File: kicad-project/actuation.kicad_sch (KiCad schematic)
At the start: 0 parts

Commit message: hw: schematic updates
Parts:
- added C? (x4): (no value), symbol Device:C
- added C?: (no value), symbol Device:C_Polarized
- added R? (x4): (no value), symbol Device:R
- added U?: (no value), symbol A4988:A4988SETTR-T
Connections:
- new net: R?.1, U?.13 (ROSC)
- new net: R?.1, U?.23 (SENSE1)
- new net: R?.1, U?.27 (SENSE2)
- new net: C?.1, U?.4 (CP1)
- new net: C?.2, U?.5 (CP2)
- new net: C?.1, U?.8 (VREG)
- new net +12V: C?.1, C?.1, U?.22 (VBB1), U?.28 (VBB2)
- new net +5V: C?.1, R?.1, U?.15 (VDD)
- new net GND: C?.2, C?.2, C?.2, R?.2, R?.2, R?.2, U?.18 (GND2), U?.3 (GND1)
- new net SLEEP: R?.2, U?.14 (~{SLEEP})
- new net VCP: C?.2, U?.6 (VCP)
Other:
- note added: "Al momento stiamo pilotando un motore unipolare Bisogna capire se questo driver supporta tali motori"
- note added: "DRV8805"
- note added: "e se bastano i pin"
- title: Actuation -> (none)

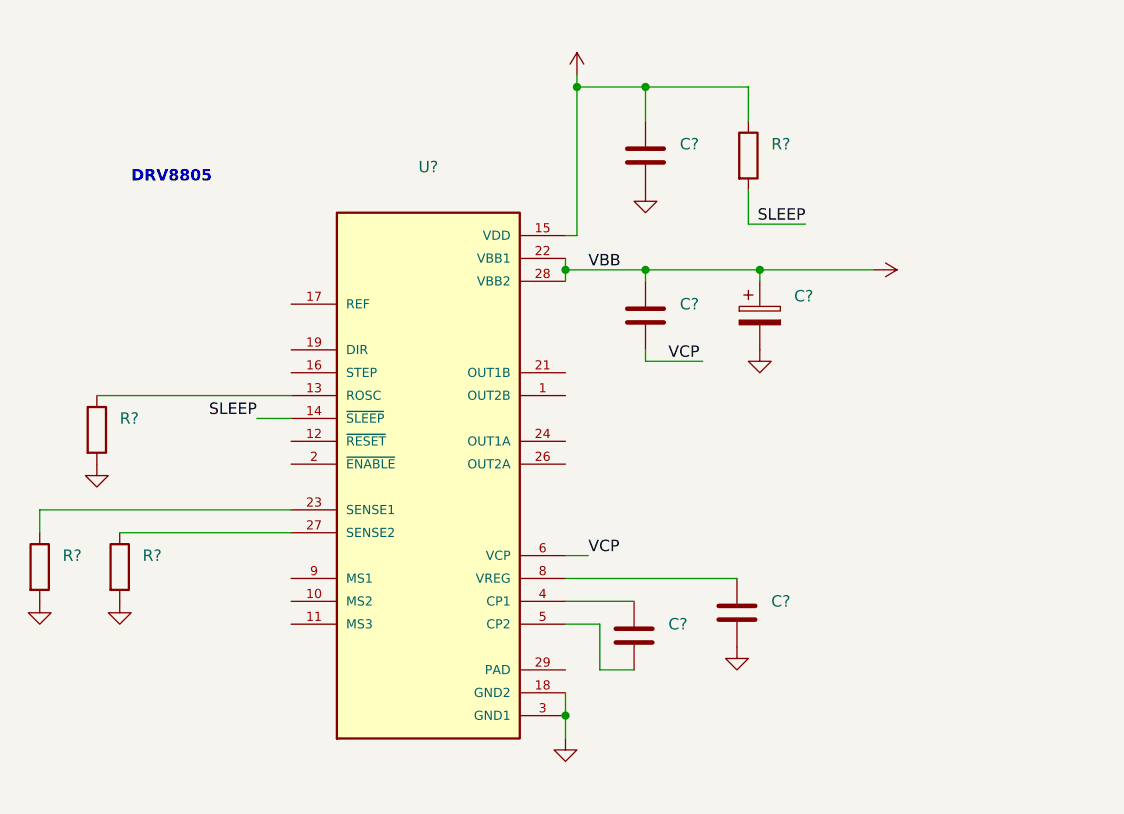
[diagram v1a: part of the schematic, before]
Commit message: hw: connect filtering capacitor near vdd pin
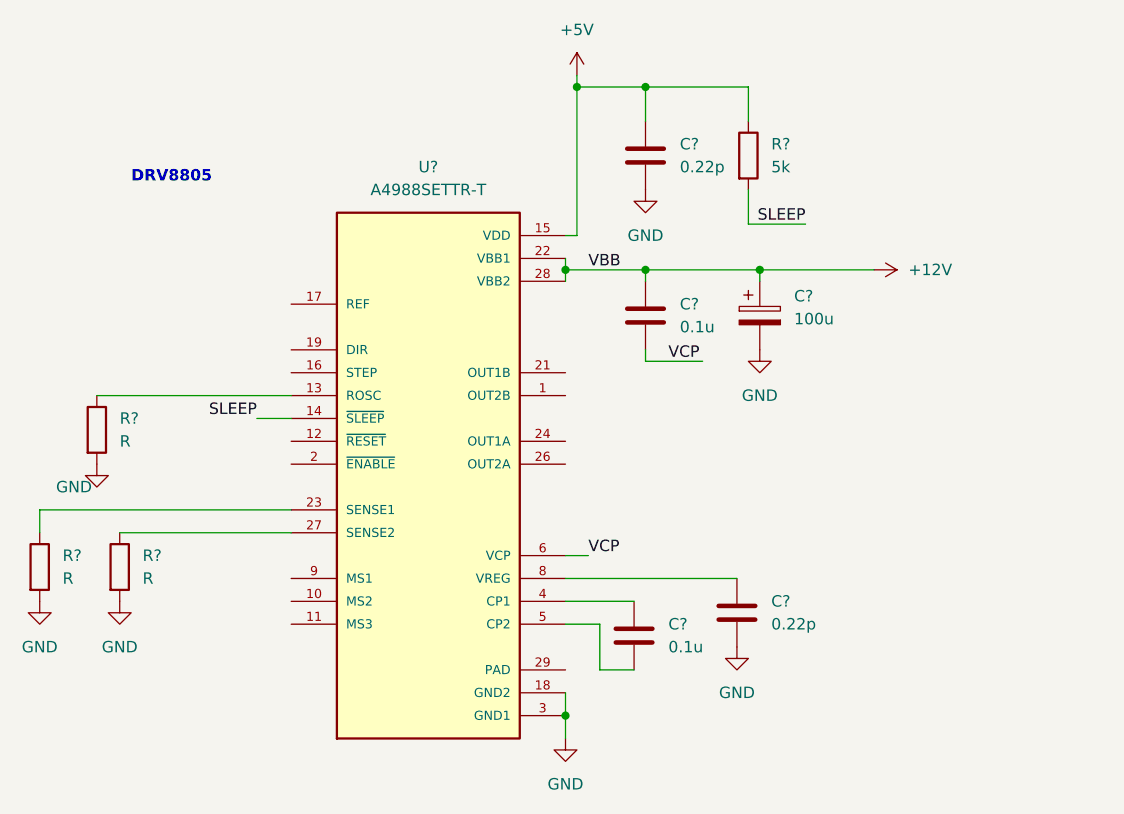
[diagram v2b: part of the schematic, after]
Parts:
- C? (x2): value (none) -> 0.22p
- C? (x2): value (none) -> 0.1u
- C?: value (none) -> 100u
- R? (x3): value (none) -> R
- R?: value (none) -> 5k
- U?: value (none) -> A4988SETTR-T; footprint (none) -> QFN50P500X500X90-29N

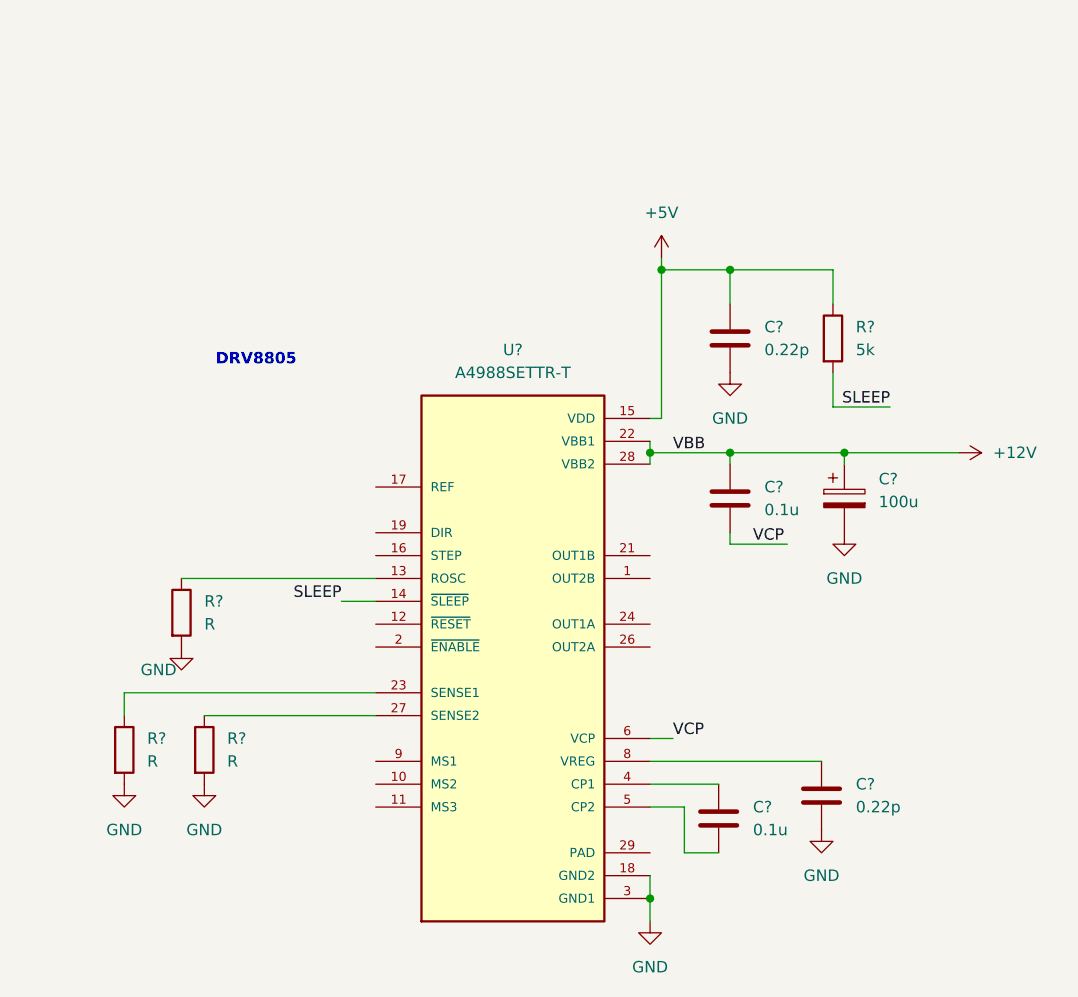
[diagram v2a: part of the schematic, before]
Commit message: hw: update schematic pt. 2
add switching enable resistor, change usb inductor to ferrite bead, add OR gate and microstepping solder jumpers to motor driver, remove i2c and backup supply solder jumper from GPS, add ferrite bead to GPS, remove limit switches and other small changes
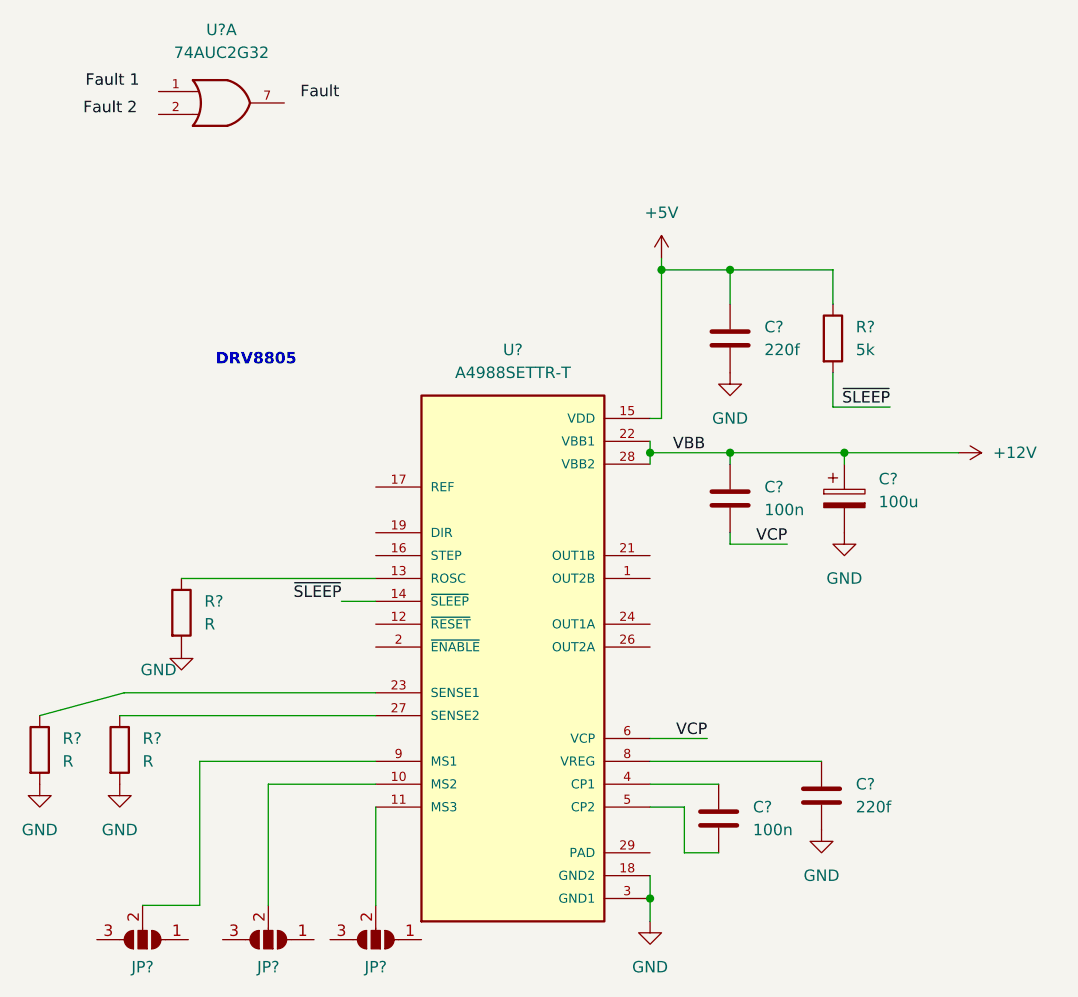
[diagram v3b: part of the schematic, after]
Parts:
- added JP? (x3): SolderJumper_3_Open, symbol Jumper:SolderJumper_3_Open
- added U?: 74AUC2G32, symbol 74xGxx:74AUC2G32
- C? (x2): value 0.22p -> 220f
- C? (x2): value 0.1u -> 100n
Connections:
- net GND: now also U?.4 (GND)
- net at U?.10 (MS2): now also JP?.2 (C)
- net at U?.11 (MS3): now also JP?.2 (C)
- net at U?.9 (MS1): now also JP?.2 (C)
- net SLEEP renamed ~{SLEEP}
- new net VCC: U?.8 (VCC)
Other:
- moved on the sheet: R?

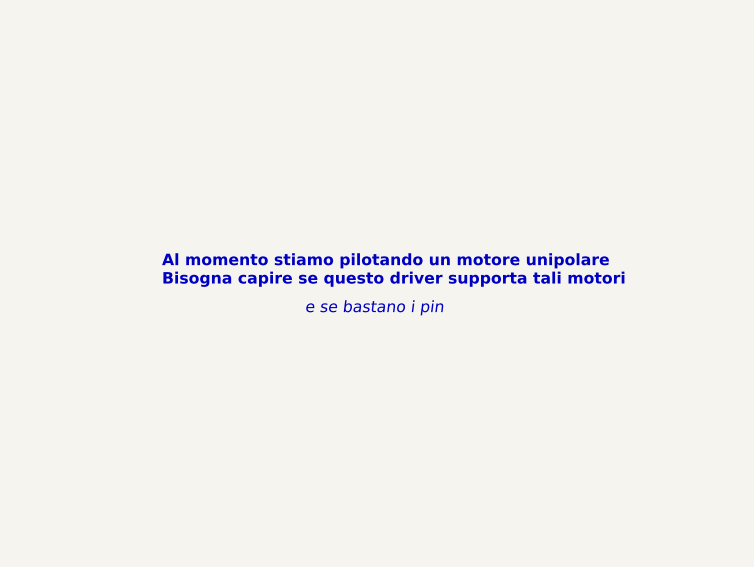
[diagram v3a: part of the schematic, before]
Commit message: hw: added MAN_NORD and TRCK_ON_OFF buttons and OLED Display
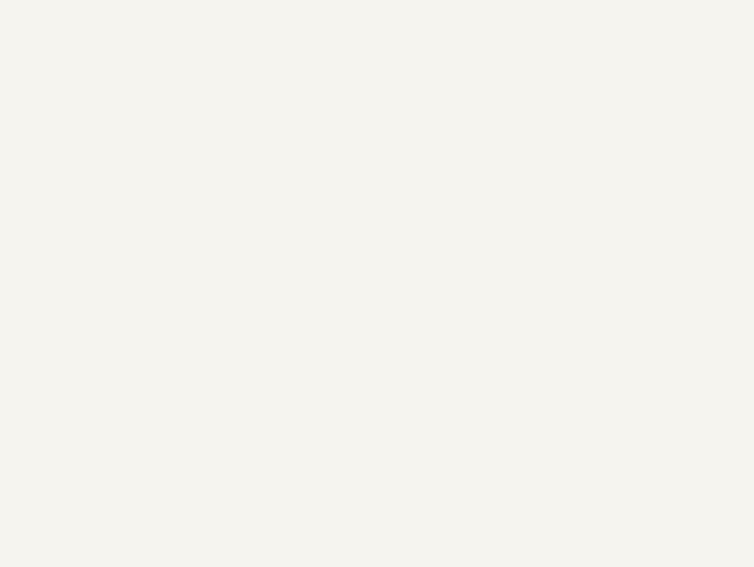
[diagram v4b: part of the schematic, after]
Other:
- note removed: "Al momento stiamo pilotando un motore unipolare Bisogna capire se questo driver supporta tali motori"
- note removed: "e se bastano i pin"

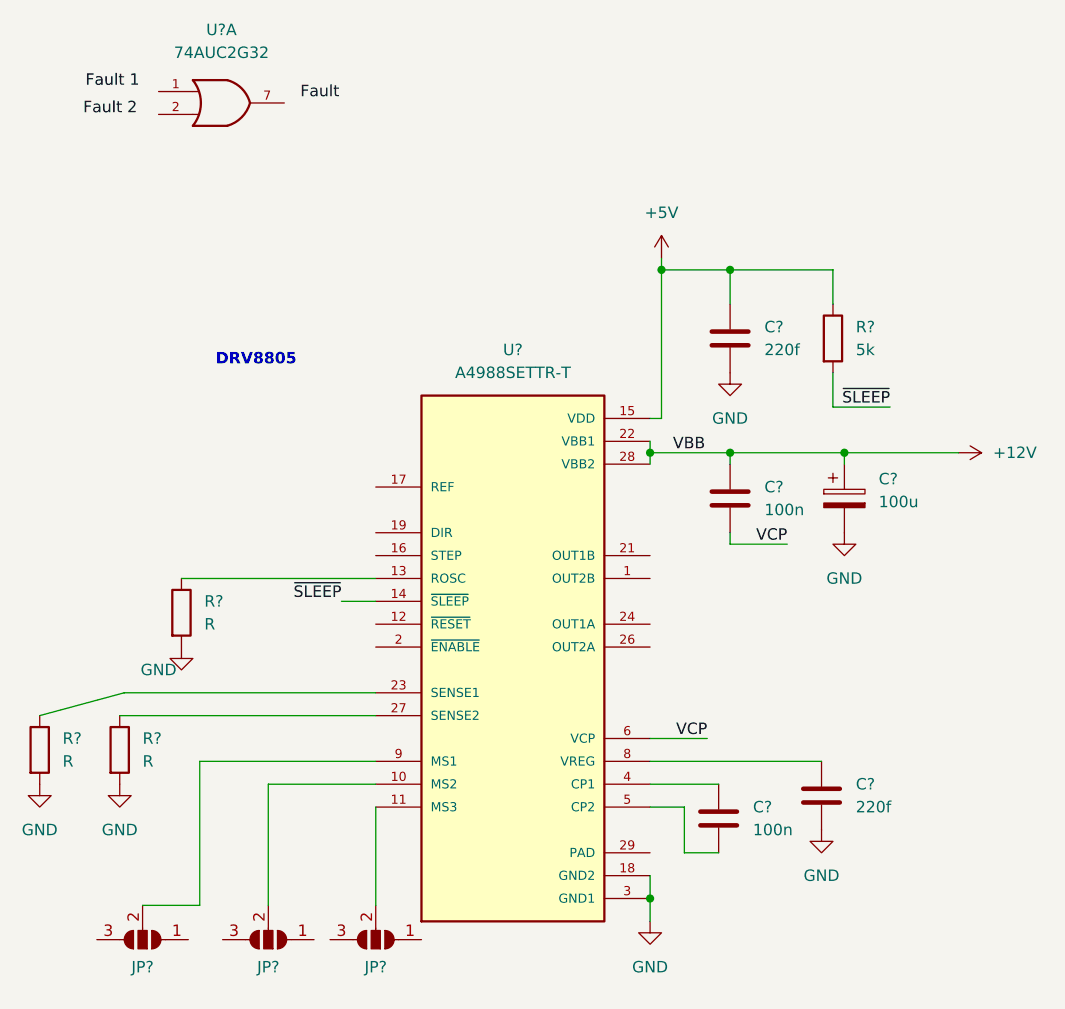
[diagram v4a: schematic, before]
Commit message: hw: set grid to 50 mils and missing labels
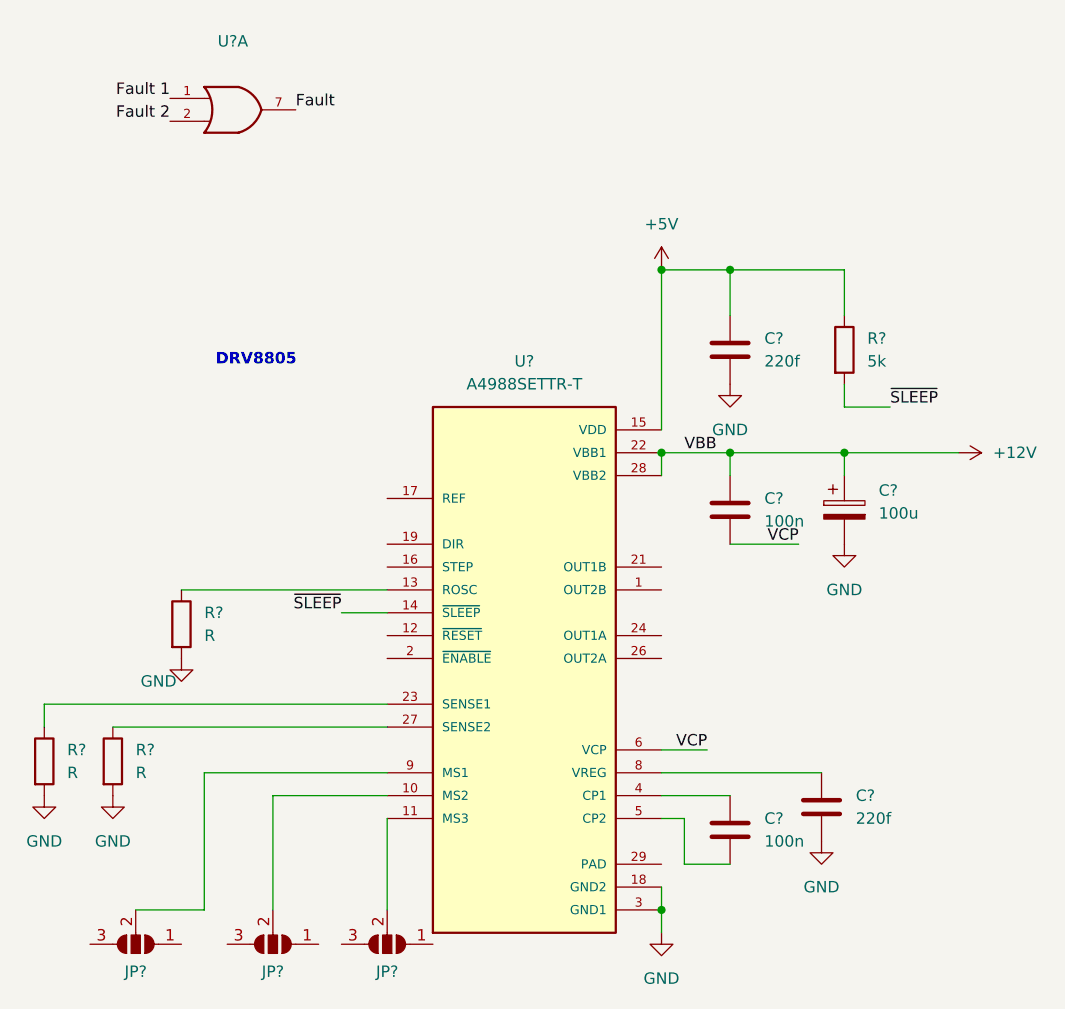
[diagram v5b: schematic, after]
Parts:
- removed U?: 74AUC2G32, symbol 74xGxx:74AUC2G32
- added U?: (no value), symbol 74xGxx:74AUC2G32
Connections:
- net Fault: now also U?.7
- net Fault 1: now also U?.1
- net Fault 2: now also U?.2
- net GND: now also U?.4 (GND)
- net VCC: now also U?.8 (VCC)
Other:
- moved on the sheet: C?, JP?, R?, U?
